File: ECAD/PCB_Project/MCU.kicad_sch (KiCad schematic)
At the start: 0 parts

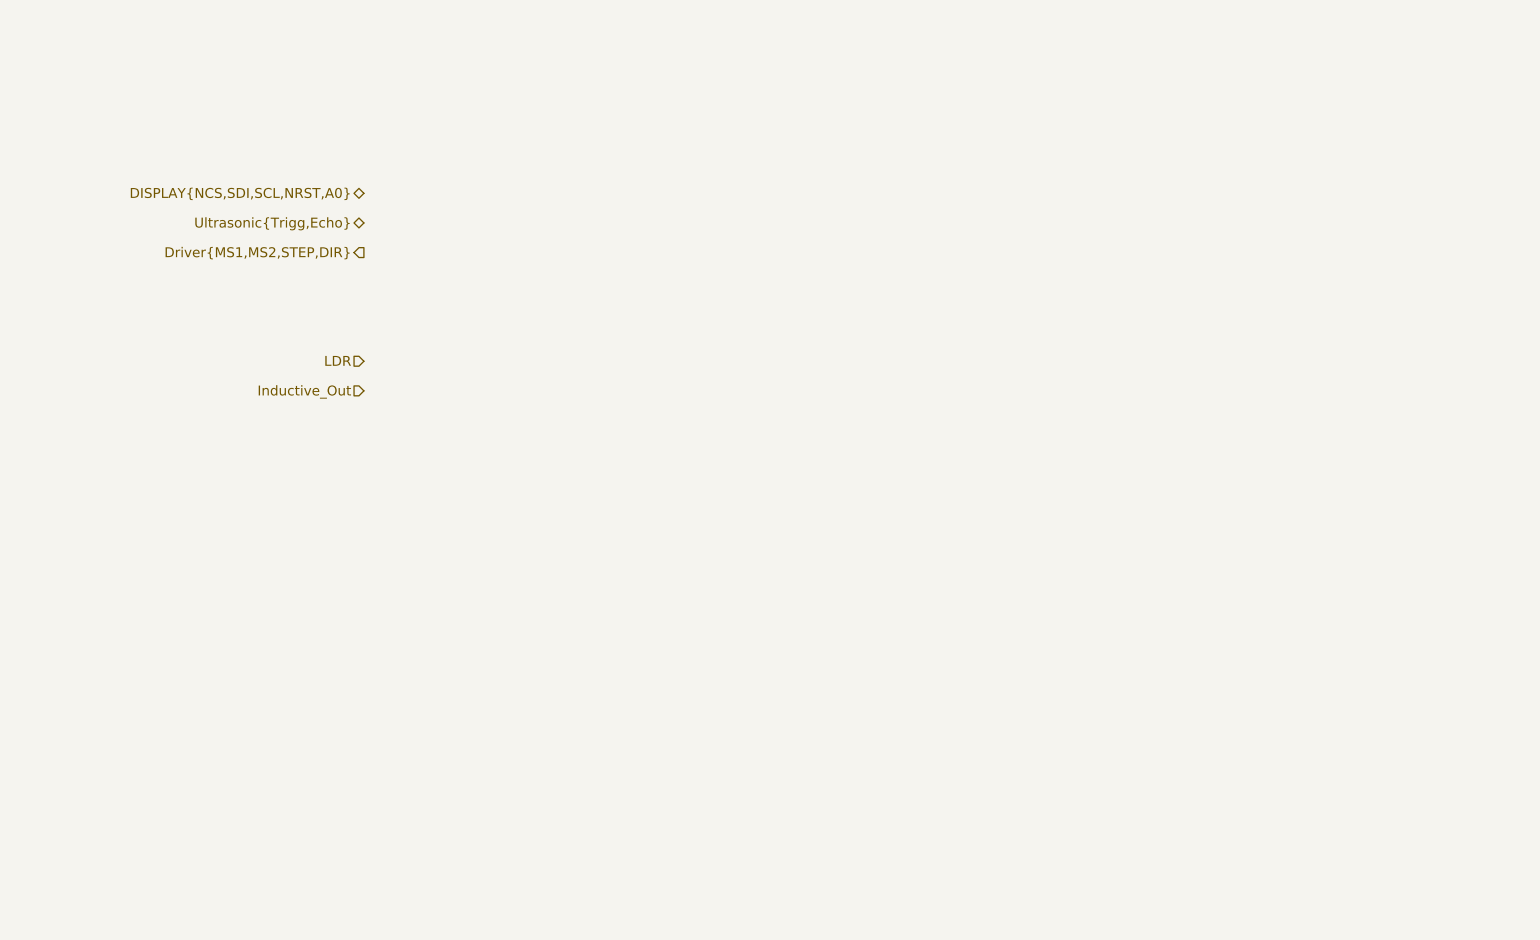
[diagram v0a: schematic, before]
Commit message: Schematic Updates
Wiring up MCU
Adding some footprints
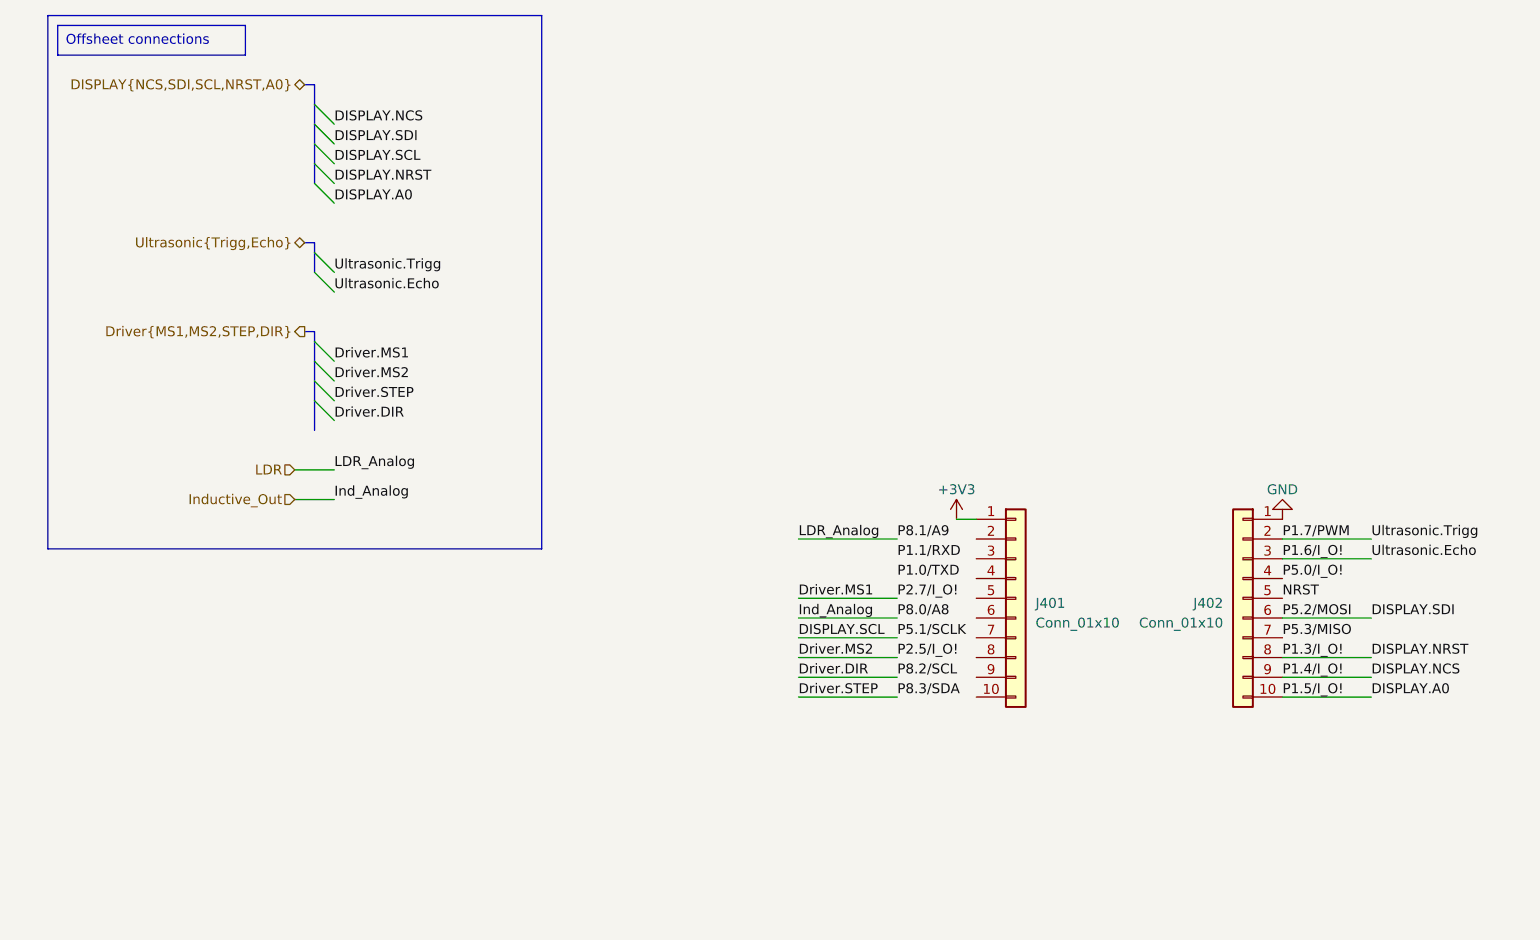
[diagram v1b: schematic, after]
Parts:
- added J401, J402: Conn_01x10, Connector_PinSocket_2.54mm:PinSocket_1x10_P2.54mm_Vertical, symbol Connector_Generic:Conn_01x10
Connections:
- new net +3V3: J401.1 (Pin_1)
- new net DISPLAY.A0: J402.10 (Pin_10)
- new net DISPLAY.NCS: J402.9 (Pin_9)
- new net DISPLAY.NRST: J402.8 (Pin_8)
- new net DISPLAY.SDI: J402.6 (Pin_6)
- new net GND: J402.1 (Pin_1)
- new net NRST: J402.5 (Pin_5)
- new net P1.6/I_O!: J402.3 (Pin_3)
- new net P1.7/PWM: J402.2 (Pin_2)
- new net P5.0/I_O!: J402.4 (Pin_4)
- new net P5.3/MISO: J402.7 (Pin_7)

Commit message: Adding Inductive Sensor Transistor
Sims + Schematics
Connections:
- net DISPLAY.SCL: now also J401.7 (Pin_7)
- net Driver.DIR: now also J401.9 (Pin_9)
- net Driver.MS1: now also J401.5 (Pin_5)
- net Driver.MS2: now also J401.8 (Pin_8)
- net Driver.STEP: now also J401.10 (Pin_10)
- net LDR: now also J401.2 (Pin_2)
- net Ind_3v3: now reaches J401.6 (Pin_6)
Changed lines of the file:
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@@
     (stroke (width 0) (type default))
   )
-  (wire (pts (xy 109.22 85.09) (xy 121.92 85.09))
+  (wire (pts (xy 109.22 85.09) (xy 132.08 85.09))
     (stroke (width 0) (type default))
   )
@@
     (stroke (width 0) (type default))
   )
-  (wire (pts (xy 109.22 95.25) (xy 121.92 95.25))
+  (wire (pts (xy 109.22 95.25) (xy 132.08 95.25))
     (stroke (width 0) (type default))
   )
@@
     (stroke (width 0) (type default))
   )
-  (wire (pts (xy 109.22 97.79) (xy 121.92 97.79))
+  (wire (pts (xy 109.22 97.79) (xy 132.08 97.79))
     (stroke (width 0) (type default))
   )
@@
     (stroke (width 0) (type default))
   )
-  (wire (pts (xy 109.22 102.87) (xy 121.92 102.87))
+  (wire (pts (xy 109.22 102.87) (xy 132.08 102.87))
     (stroke (width 0) (type default))
   )
@@
     (stroke (width 0) (type default))
   )
-  (wire (pts (xy 109.22 100.33) (xy 121.92 100.33))
+  (wire (pts (xy 109.22 100.33) (xy 132.08 100.33))
     (stroke (width 0) (type default))
   )
@@
     (stroke (width 0) (type default))
   )
-  (wire (pts (xy 109.22 105.41) (xy 121.92 105.41))
+  (wire (pts (xy 109.22 105.41) (xy 132.08 105.41))
     (stroke (width 0) (type default))
   )
@@
     (stroke (width 0) (type default))
   )
-  (wire (pts (xy 109.22 92.71) (xy 121.92 92.71))
+  (wire (pts (xy 109.22 92.71) (xy 132.08 92.71))
     (stroke (width 0) (type default))
   )
@@
     (effects (font (size 1.27 1.27)) (justify left bottom))
   )
-  (label "Driver.MS2" (at 49.53 64.77 0)
+  (label "Driver.MS2" (at 49.53 64.77 0) (fields_autoplaced)
     (effects (font (size 1.27 1.27)) (justify left bottom))
   )
@@
     (effects (font (size 1.27 1.27)) (justify left bottom))
   )
-  (label "DISPLAY.NCS" (at 49.53 31.75 0)
+  (label "DISPLAY.NCS" (at 49.53 31.75 0) (fields_autoplaced)
     (effects (font (size 1.27 1.27)) (justify left bottom))
   )
@@
     (effects (font (size 1.27 1.27)) (justify left bottom))
   )
-  (label "Driver.STEP" (at 49.53 67.31 0)
-    (effects (font (size 1.27 1.27)) (justify left bottom))
-  )
-  (label "DISPLAY.SDI" (at 49.53 34.29 0)
-    (effects (font (size 1.27 1.27)) (justify left bottom))
-  )
-  (label "Driver.DIR" (at 49.53 69.85 0)
+  (label "Driver.STEP" (at 49.53 67.31 0) (fields_autoplaced)
+    (effects (font (size 1.27 1.27)) (justify left bottom))
+  )
+  (label "DISPLAY.SDI" (at 49.53 34.29 0) (fields_autoplaced)
+    (effects (font (size 1.27 1.27)) (justify left bottom))
+  )
+  (label "Driver.DIR" (at 49.53 69.85 0) (fields_autoplaced)
     (effects (font (size 1.27 1.27)) (justify left bottom))
   )
@@
     (effects (font (size 1.27 1.27)) (justify left bottom))
   )
-  (label "DISPLAY.NRST" (at 49.53 39.37 0)
-    (effects (font (size 1.27 1.27)) (justify left bottom))
-  )
-  (label "Driver.MS1" (at 49.53 62.23 0)
+  (label "DISPLAY.NRST" (at 49.53 39.37 0) (fields_autoplaced)
+    (effects (font (size 1.27 1.27)) (justify left bottom))
+  )
+  (label "Driver.MS1" (at 49.53 62.23 0) (fields_autoplaced)
     (effects (font (size 1.27 1.27)) (justify left bottom))
   )
@@
     (effects (font (size 1.27 1.27)) (justify left bottom))
   )
-  (label "Ultrasonic.Trigg" (at 49.53 50.8 0)
+  (label "Ultrasonic.Trigg" (at 49.53 50.8 0) (fields_autoplaced)
     (effects (font (size 1.27 1.27)) (justify left bottom))
   )
@@
     (effects (font (size 1.27 1.27)) (justify left bottom))
   )
-  (label "DISPLAY.SDI" (at 182.88 95.25 0)
+  (label "DISPLAY.SDI" (at 182.88 95.25 0) (fields_autoplaced)
     (effects (font (size 1.27 1.27)) (justify left bottom))
   )
@@
     (effects (font (size 1.27 1.27)) (justify left bottom))
   )
-  (label "DISPLAY.SCL" (at 49.53 36.83 0)
+  (label "DISPLAY.SCL" (at 49.53 36.83 0) (fields_autoplaced)
     (effects (font (size 1.27 1.27)) (justify left bottom))
   )
@@
     (effects (font (size 1.27 1.27)) (justify left bottom))
   )
-  (label "Ultrasonic.Echo" (at 49.53 53.34 0)
+  (label "Ultrasonic.Echo" (at 49.53 53.34 0) (fields_autoplaced)
     (effects (font (size 1.27 1.27)) (justify left bottom))
   )
@@
     (effects (font (size 1.27 1.27)) (justify left bottom))
   )
-  (label "DISPLAY.A0" (at 49.53 41.91 0)
+  (label "DISPLAY.A0" (at 49.53 41.91 0) (fields_autoplaced)
     (effects (font (size 1.27 1.27)) (justify left bottom))
   )
@@
     (effects (font (size 1.27 1.27)) (justify right))
   )
-  (hierarchical_label "Inductive_Out" (shape input) (at 44.45 80.01 180) (fields_autoplaced)
-    (effects (font (size 1.27 1.27)) (justify right))
-  )
+  (hierarchical_label "Ind_3v3" (shape input) (at 44.45 80.01 180) (fields_autoplaced)
+    (effects (font (size 1.27 1.27)) (justify right))
+  )

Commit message: First PCB Draft
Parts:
- added J403: Conn_01x02, Connector_PinHeader_2.54mm:PinHeader_1x02_P2.54mm_Vertical, symbol Connector_Generic:Conn_01x02
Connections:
- net P5.3/MISO is gone; now on net DISPLAY.A0: J402.7 (Pin_7)
- net DISPLAY.A0: no longer J402.10 (Pin_10)
- net GND: now also J403.1 (Pin_1)
- net P1.6/I_O! renamed SG90_PWM
- new net +5V: J403.2 (Pin_2)
- new net P1.5/I_O!: J402.10 (Pin_10)
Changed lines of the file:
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@@
+    (stroke (width 0) (type default))
+  )
+  (wire (pts (xy 171.45 90.17) (xy 182.88 90.17))
     (stroke (width 0) (type default))
   )
@@
     (stroke (width 0) (type default))
   )
+  (wire (pts (xy 146.05 85.09) (xy 149.225 85.09))
+    (stroke (width 0) (type default))
+  )
   (bus (pts (xy 46.99 62.23) (xy 46.99 64.77))
     (stroke (width 0) (type default))
@@
     (stroke (width 0) (type default))
   )
+  (wire (pts (xy 44.45 83.82) (xy 49.53 83.82))
+    (stroke (width 0) (type default))
+  )
   (bus (pts (xy 46.99 67.31) (xy 46.99 71.12))
     (stroke (width 0) (type default))
   )
+  (wire (pts (xy 146.05 82.55) (xy 149.225 82.55))
+    (stroke (width 0) (type default))
+  )
+  (wire (pts (xy 171.45 87.63) (xy 182.88 87.63))
+    (stroke (width 0) (type default))
+  )
   (wire (pts (xy 109.22 95.25) (xy 132.08 95.25))
     (stroke (width 0) (type default))
@@
     (stroke (width 0) (type default))
   )
+  (wire (pts (xy 171.45 97.79) (xy 182.88 97.79))
+    (stroke (width 0) (type default))
+  )
   (wire (pts (xy 171.45 85.09) (xy 182.88 85.09))
     (stroke (width 0) (type default))
@@
     (stroke (width 0) (type default))
   )
-  (wire (pts (xy 171.45 87.63) (xy 182.88 87.63))
-    (stroke (width 0) (type default))
-  )
   (wire (pts (xy 109.22 105.41) (xy 132.08 105.41))
     (stroke (width 0) (type default))
@@
     (stroke (width 0) (type default))
   )
-  (rectangle (start 12.7 17.78) (end 76.2 86.36)
+  (rectangle (start 12.7 17.78) (end 76.2 95.25)
     (stroke (width 0) (type default))
     (fill (type none))
@@
     (effects (font (size 1.27 1.27)) (justify left bottom))
   )
+  (label "DISPLAY.A0" (at 182.88 97.79 0) (fields_autoplaced)
+    (effects (font (size 1.27 1.27)) (justify left bottom))
+  )
   (label "P8.1{slash}A9" (at 121.92 85.09 0) (fields_autoplaced)
     (effects (font (size 1.27 1.27)) (justify left bottom))
@@
     (effects (font (size 1.27 1.27)) (justify left bottom))
   )
-  (label "DISPLAY.A0" (at 182.88 105.41 0) (fields_autoplaced)
+  (label "SG90_PWM" (at 182.88 87.63 0) (fields_autoplaced)
     (effects (font (size 1.27 1.27)) (justify left bottom))
   )
@@
     (effects (font (size 1.27 1.27)) (justify left bottom))
   )
-  (label "Ultrasonic.Echo" (at 182.88 87.63 0) (fields_autoplaced)
+  (label "Ultrasonic.Echo" (at 182.88 90.17 0) (fields_autoplaced)
     (effects (font (size 1.27 1.27)) (justify left bottom))
   )
@@
     (effects (font (size 1.27 1.27)) (justify left bottom))
   )
+  (label "SG90_PWM" (at 49.53 83.82 0) (fields_autoplaced)
+    (effects (font (size 1.27 1.27)) (justify left bottom))
+  )
   (label "P2.7{slash}I_O!" (at 121.92 92.71 0) (fields_autoplaced)
     (effects (font (size 1.27 1.27)) (justify left bottom))
@@
   )
   (hierarchical_label "LDR" (shape input) (at 44.45 76.2 180) (fields_autoplaced)
+    (effects (font (size 1.27 1.27)) (justify right))
+  )
+  (hierarchical_label "SG90_PWM" (shape output) (at 44.45 83.82 180) (fields_autoplaced)
     (effects (font (size 1.27 1.27)) (justify right))
   )
@@
     )
   )
+  (symbol (lib_id "power:GND") (at 149.225 85.09 0) (unit 1)
+    (in_bom yes) (on_board yes) (dnp no) (fields_autoplaced)
+    (property "Reference" "#PWR0404" (at 149.225 91.44 0)
+      (effects (font (size 1.27 1.27)) hide)
+    )
+    (property "Value" "GND" (at 149.225 90.17 0)
+      (effects (font (size 1.27 1.27)))
+    )
+    (property "Footprint" "" (at 149.225 85.09 0)
+      (effects (font (size 1.27 1.27)) hide)
+    )
+    (property "Datasheet" "" (at 149.225 85.09 0)
+      (effects (font (size 1.27 1.27)) hide)
+    )
+    (pin "1")
+    (instances
+      (project "PCB_Project"
+        (path "/96782006-a72a-4cbb-9ab4-56557ee1053d/0419be2b-5ee6-4a8c-8789-c753ffca51aa"
+          (reference "#PWR0404") (unit 1)
+        )
+      )
+    )
+  )
   (symbol (lib_id "power:GND") (at 171.45 82.55 180) (unit 1)
     (in_bom yes) (on_board yes) (dnp no) (fields_autoplaced)
@@
         )
       )
+    )
+  )
+  (symbol (lib_id "power:+5V") (at 149.225 82.55 0) (unit 1)
+    (in_bom yes) (on_board yes) (dnp no) (fields_autoplaced)
+    (property "Reference" "#PWR0403" (at 149.225 86.36 0)
+      (effects (font (size 1.27 1.27)) hide)
+    )
+    (property "Value" "+5V" (at 149.225 78.74 0)
+      (effects (font (size 1.27 1.27)))
+    )
+    (property "Footprint" "" (at 149.225 82.55 0)
+      (effects (font (size 1.27 1.27)) hide)
+    )
+    (property "Datasheet" "" (at 149.225 82.55 0)
+      (effects (font (size 1.27 1.27)) hide)
+    )
+    (pin "1")
+    (instances
+      (project "PCB_Project"
+        (path "/96782006-a72a-4cbb-9ab4-56557ee1053d/0419be2b-5ee6-4a8c-8789-c753ffca51aa"
+          (reference "#PWR0403") (unit 1)
+        )
+      )
+    )
+  )
+  (symbol (lib_id "Connector_Generic:Conn_01x02") (at 140.97 85.09 180) (unit 1)
+    (in_bom yes) (on_board yes) (dnp no) (fields_autoplaced)
+    (property "Reference" "J403" (at 140.97 77.47 0)
+      (effects (font (size 1.27 1.27)))
+    )
+    (property "Value" "Conn_01x02" (at 140.97 80.01 0)
+      (effects (font (size 1.27 1.27)))
+    )
+    (property "Footprint" "Connector_PinHeader_2.54mm:PinHeader_1x02_P2.54mm_Vertical" (at 140.97 85.09 0)
+      (effects (font (size 1.27 1.27)) hide)
+    )
+    (property "Datasheet" "~" (at 140.97 85.09 0)
+      (effects (font (size 1.27 1.27)) hide)
+    )
+    (pin "1")
+    (pin "2")
+    (instances
+      (project "PCB_Project"
+        (path "/96782006-a72a-4cbb-9ab4-56557ee1053d/0419be2b-5ee6-4a8c-8789-c753ffca51aa"
+          (reference "J403") (unit 1)
+        )
+      )

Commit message: Final PCB
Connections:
- net Driver.MS1 renamed P2.7/I_O!
- net Driver.MS2 renamed P2.5/I_O!
- no-connect marks 0 -> 3
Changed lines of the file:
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@@
 	(generator_version "8.0")
 	(paper "A4")
+	(no_connect
+		(at 109.22 92.71)
+	)
+	(no_connect
+		(at 182.88 105.41)
+	)
+	(no_connect
+		(at 109.22 100.33)
+	)
 	(bus_entry
-		(at 46.99 67.31)
+		(at 46.99 62.23)
 		(size 2.54 2.54)
 		(stroke
@@
 	)
 	(bus_entry
-		(at 46.99 64.77)
+		(at 46.99 59.69)
 		(size 2.54 2.54)
 		(stroke
@@
 	)
 	(bus_entry
-		(at 46.99 59.69)
-		(size 2.54 2.54)
-		(stroke
-			(width 0)
-			(type default)
-		)
-	)
-	(bus_entry
 		(at 46.99 31.75)
 		(size 2.54 2.54)
@@
 		)
 	)
-	(bus_entry
-		(at 46.99 62.23)
-		(size 2.54 2.54)
-		(stroke
-			(width 0)
-			(type default)
-		)
-	)
 	(wire
 		(pts
@@
 	(bus
 		(pts
+			(xy 46.99 58.42) (xy 46.99 59.69)
+		)
+		(stroke
+			(width 0)
+			(type default)
+		)
+	)
+	(wire
+		(pts
+			(xy 146.05 85.09) (xy 149.225 85.09)
+		)
+		(stroke
+			(width 0)
+			(type default)
+		)
+	)
+	(wire
+		(pts
+			(xy 171.45 95.25) (xy 182.88 95.25)
+		)
+		(stroke
+			(width 0)
+			(type default)
+		)
+	)
+	(wire
+		(pts
+			(xy 44.45 83.82) (xy 49.53 83.82)
+		)
+		(stroke
+			(width 0)
+			(type default)
+		)
+	)
+	(wire
+		(pts
+			(xy 146.05 82.55) (xy 149.225 82.55)
+		)
+		(stroke
+			(width 0)
+			(type default)
+		)
+	)
+	(wire
+		(pts
+			(xy 171.45 87.63) (xy 182.88 87.63)
+		)
+		(stroke
+			(width 0)
+			(type default)
+		)
+	)
+	(wire
+		(pts
+			(xy 109.22 95.25) (xy 132.08 95.25)
+		)
+		(stroke
+			(width 0)
+			(type default)
+		)
+	)
+	(bus
+		(pts
+			(xy 45.72 46.99) (xy 46.99 46.99)
+		)
+		(stroke
+			(width 0)
+			(type default)
+		)
+	)
+	(wire
+		(pts
+			(xy 171.45 97.79) (xy 182.88 97.79)
+		)
+		(stroke
+			(width 0)
+			(type default)
+		)
+	)
+	(wire
+		(pts
+			(xy 171.45 85.09) (xy 182.88 85.09)
+		)
+		(stroke
+			(width 0)
+			(type default)
+		)
+	)
+	(wire
+		(pts
+			(xy 109.22 97.79) (xy 132.08 97.79)
+		)
+		(stroke
+			(width 0)
+			(type default)
+		)
+	)
+	(wire
+		(pts
+			(xy 171.45 100.33) (xy 182.88 100.33)
+		)
+		(stroke
+			(width 0)
+			(type default)
+		)
+	)
+	(bus
+		(pts
+			(xy 46.99 34.29) (xy 46.99 36.83)
+		)
+		(stroke
+			(width 0)
+			(type default)
+		)
+	)
+	(bus
+		(pts
 			(xy 46.99 59.69) (xy 46.99 62.23)
-		)
-		(stroke
-			(width 0)
-			(type default)
-		)
-	)
-	(wire
-		(pts
-			(xy 146.05 85.09) (xy 149.225 85.09)
-		)
-		(stroke
-			(width 0)
-			(type default)
-		)
-	)
-	(bus
-		(pts
-			(xy 46.99 62.23) (xy 46.99 64.77)
-		)
-		(stroke
-			(width 0)
-			(type default)
-		)
-	)
-	(wire
-		(pts
-			(xy 171.45 95.25) (xy 182.88 95.25)
-		)
-		(stroke
-			(width 0)
-			(type default)
-		)
-	)
-	(wire
-		(pts
-			(xy 44.45 83.82) (xy 49.53 83.82)
-		)
-		(stroke
-			(width 0)
-			(type default)
-		)
-	)
-	(bus
-		(pts
-			(xy 46.99 67.31) (xy 46.99 71.12)
-		)
-		(stroke
-			(width 0)
-			(type default)
-		)
-	)
-	(wire
-		(pts
-			(xy 146.05 82.55) (xy 149.225 82.55)
-		)
-		(stroke
-			(width 0)
-			(type default)
-		)
-	)
-	(wire
-		(pts
-			(xy 171.45 87.63) (xy 182.88 87.63)
-		)
-		(stroke
-			(width 0)
-			(type default)
-		)
-	)
-	(wire
-		(pts
-			(xy 109.22 95.25) (xy 132.08 95.25)
-		)
-		(stroke
-			(width 0)
-			(type default)
-		)
-	)
-	(bus
-		(pts
-			(xy 45.72 46.99) (xy 46.99 46.99)
-		)
-		(stroke
-			(width 0)
-			(type default)
-		)
-	)
-	(wire
-		(pts
-			(xy 171.45 97.79) (xy 182.88 97.79)
-		)
-		(stroke
-			(width 0)
-			(type default)
-		)
-	)
-	(wire
-		(pts
-			(xy 171.45 85.09) (xy 182.88 85.09)
-		)
-		(stroke
-			(width 0)
-			(type default)
-		)
-	)
-	(wire
-		(pts
-			(xy 109.22 97.79) (xy 132.08 97.79)
-		)
-		(stroke
-			(width 0)
-			(type default)
-		)
-	)
-	(wire
-		(pts
-			(xy 171.45 100.33) (xy 182.88 100.33)
-		)
-		(stroke
-			(width 0)
-			(type default)
-		)
-	)
-	(bus
-		(pts
-			(xy 46.99 34.29) (xy 46.99 36.83)
-		)
-		(stroke
-			(width 0)
-			(type default)
-		)
-	)
-	(bus
-		(pts
-			(xy 46.99 58.42) (xy 46.99 59.69)
-		)
-		(stroke
-			(width 0)
-			(type default)
-		)
-	)
-	(bus
-		(pts
-			(xy 46.99 64.77) (xy 46.99 67.31)
 		)
 		(stroke
@@
 		)
 	)
-	(label "Driver.MS2"
-		(at 49.53 64.77 0)
-		(fields_autoplaced yes)
-		(effects
-			(font
-				(size 1.27 1.27)
-			)
-			(justify left bottom)
-		)
-	)
 	(label "P8.0{slash}A8"
 		(at 121.92 95.25 0)
@@
 		)
 	)
-	(label "Driver.MS2"
-		(at 109.22 100.33 0)
-		(fields_autoplaced yes)
-		(effects
-			(font
-				(size 1.27 1.27)
-			)
-			(justify left bottom)
-		)
-	)
 	(label "DISPLAY.NCS"
 		(at 49.53 31.75 0)
@@
 	)
 	(label "Driver.STEP"
-		(at 49.53 67.31 0)
+		(at 49.53 62.23 0)
 		(fields_autoplaced yes)
 		(effects
@@
 	)
 	(label "Driver.DIR"
-		(at 49.53 69.85 0)
+		(at 49.53 64.77 0)
 		(fields_autoplaced yes)
 		(effects
@@
 		)
 	)
-	(label "Driver.MS1"
-		(at 49.53 62.23 0)
-		(fields_autoplaced yes)
-		(effects
-			(font
-				(size 1.27 1.27)
-			)
-			(justify left bottom)
-		)
-	)
 	(label "P1.1{slash}RXD"
 		(at 121.92 87.63 0)
@@
 	(label "P2.5{slash}I_O!"
 		(at 121.92 100.33 0)
-		(fields_autoplaced yes)
-		(effects
-			(font
-				(size 1.27 1.27)
-			)
-			(justify left bottom)
-		)
-	)
-	(label "Driver.MS1"
-		(at 109.22 92.71 0)
 		(fields_autoplaced yes)
 		(effects
@@
 		)
 	)
-	(hierarchical_label "Driver{MS1,MS2,STEP,DIR}"
+	(hierarchical_label "Driver{STEP,DIR}"
 		(shape output)
 		(at 45.72 58.42 180)
